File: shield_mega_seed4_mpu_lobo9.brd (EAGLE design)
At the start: 99.4 x 72.4 mm, 35 parts, among them U1 GY-521MPU6050

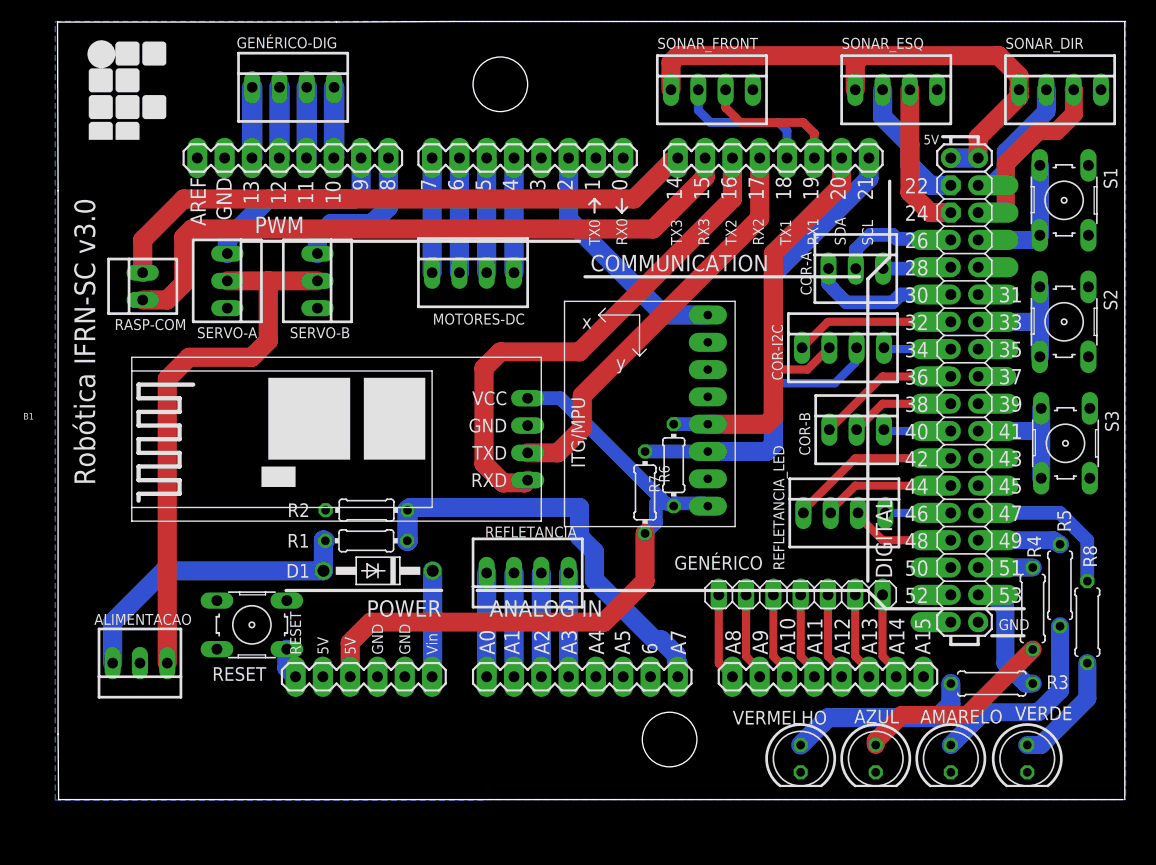
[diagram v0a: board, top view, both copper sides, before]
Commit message: Mudança de botões
mudança de posição nos botões
adição de conectores genéricos
adição de um quarto conector para sonares
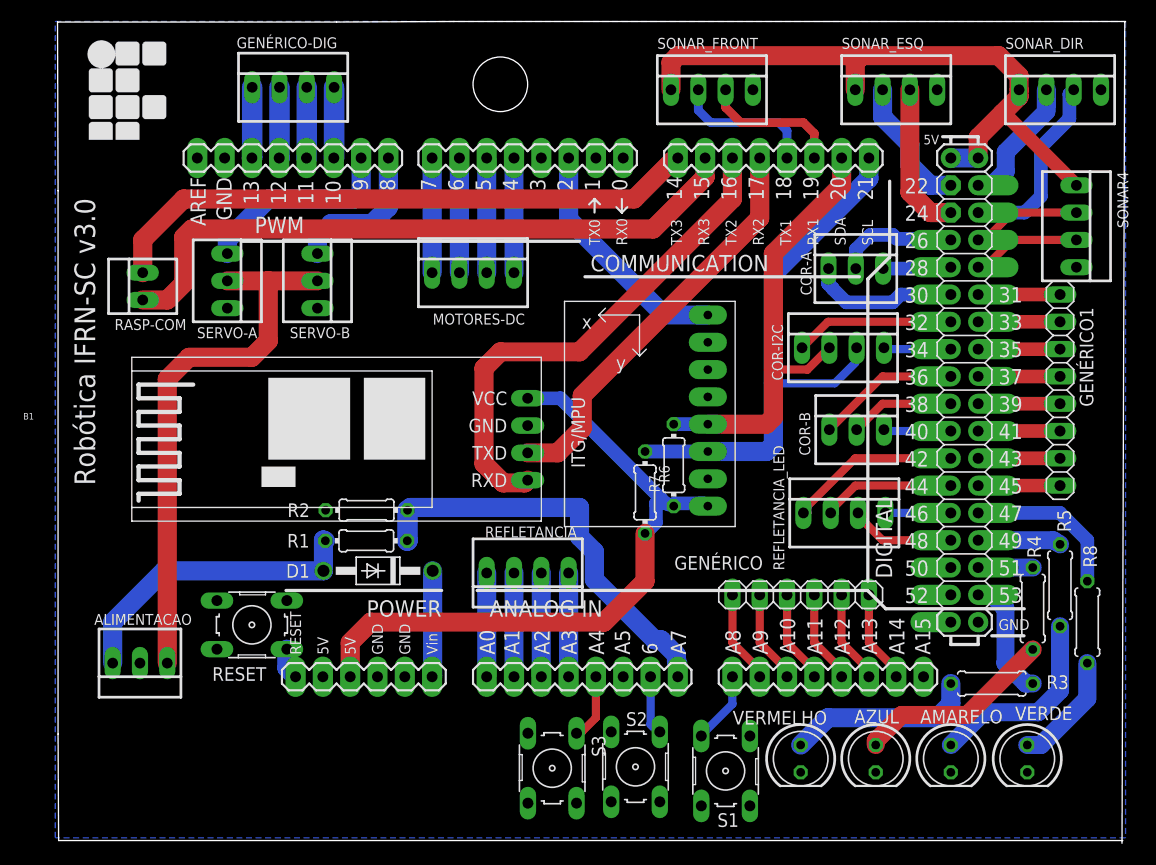
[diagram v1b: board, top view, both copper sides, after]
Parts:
- added GENÉRICO1: (no value), pinhead:1X08
- added SONAR4: (no value), con-molex:22-23-2041
- GENÉRICO: device pinhead:1X07 -> pinhead:1X06
- moved S1 61.7 mm to (61.6, 11.6), turned to 90 degrees
- moved S2 57.5 mm to (53.2, 11.9)
- moved S3 56.5 mm to (45.5, 11.8)
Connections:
- new net N$59: B1.A4, S3.1
- new net N$60: B1.31, GENÉRICO1.1
- new net N$61: B1.33, GENÉRICO1.2
- new net N$62: B1.35, GENÉRICO1.3
- new net N$63: B1.37, GENÉRICO1.4
- new net N$64: B1.39, GENÉRICO1.5
- new net N$65: B1.41, GENÉRICO1.6
- new net N$66: B1.43, GENÉRICO1.7
- new net N$67: B1.45, GENÉRICO1.8
- net 5V: now also SONAR4.1
- net GND: now also S1.3, S1.4, S2.3, S2.4, S3.3, S3.4, SONAR4.4; no longer S1.1, S1.2, S2.1, S2.2, S3.1, S3.2
- net N$27: now also B1.27, SONAR4.2; no longer B1.33, S2.3, S2.4
- net N$28: now also B1.A6, S2.1; no longer B1.27, S1.3, S1.4
- net N$30: now also B1.29, SONAR4.3; no longer B1.41, S3.3, S3.4
- net N$52: now also B1.A14, GENÉRICO.6; no longer B1.A8, GENÉRICO.1
- net N$53: now also B1.A13, GENÉRICO.5; no longer B1.A9, GENÉRICO.2
- net N$54: now also B1.A12, GENÉRICO.4; no longer B1.A10, GENÉRICO.3
- net N$55: now also GENÉRICO.3; no longer GENÉRICO.4
- net N$56: now also B1.A10, GENÉRICO.2; no longer B1.A12, GENÉRICO.5
- net N$57: now also B1.A9, GENÉRICO.1; no longer B1.A13, GENÉRICO.6
- net N$58: now also B1.A8, S1.2; no longer B1.A14, GENÉRICO.7
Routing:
- net 5V: track 51.0 -> 60.7 mm
- net N$67: track 0.00 -> 7.62 mm
- net N$66: track 0.00 -> 7.62 mm
- net N$65: track 0.00 -> 7.62 mm
- net N$64: track 0.00 -> 7.62 mm
- net N$63: track 0.00 -> 7.62 mm
- net N$62: track 0.00 -> 7.62 mm
- net N$61: track 0.00 -> 7.62 mm
- net N$60: track 0.00 -> 7.62 mm
- net N$28: track 12.4 -> 5.58 mm
- net N$59: track 0.00 -> 6.17 mm
- net N$30: track 12.4 -> 10.2 mm
- net N$27: track 12.3 -> 10.2 mm
- net N$58: track 8.15 -> 6.69 mm
- net N$56: track 8.15 -> 8.67 mm
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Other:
- board size 99.4 x 72.4 mm -> 99.4 x 76.5 mm

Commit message: Adição de conectores
Adição dos conectores de alimentação genéricos
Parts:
- added ALIMENTAÇÃO: (no value), pinhead:2X06
- moved GENÉRICO1 1.02 mm to (93.7, 47.0)
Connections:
- removed net N$32: B1.VIN, D1.C
- new net +3V3: ALIMENTAÇÃO.5, ALIMENTAÇÃO.6, B1.3.3V
- new net V+: ALIMENTAÇÃO.11, ALIMENTAÇÃO.12, B1.VIN, D1.C
- net +5V/1: now also ALIMENTAÇÃO.7, ALIMENTAÇÃO.8
- net GND: now also ALIMENTAÇÃO.10, ALIMENTAÇÃO.9
- net VDD: now also ALIMENTAÇÃO.3, ALIMENTAÇÃO.4
- net VIN: now also ALIMENTAÇÃO.1, ALIMENTAÇÃO.2
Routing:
- net VIN: track 28.5 -> 48.6 mm
- net V+: track 0.00 -> 18.8 mm
- net VDD: track 51.3 -> 69.1 mm
- net N$32: track 9.88 -> 0.00 mm
- net +5V/1: track 62.4 -> 70.2 mm
- net GND: track 0.38 -> 8.26 mm
- net +3V3: track 0.00 -> 7.87 mm
- net N$67: track 7.62 -> 8.64 mm
- net N$66: track 7.62 -> 8.64 mm
- net N$65: track 7.62 -> 8.64 mm
- net N$64: track 7.62 -> 8.64 mm
- net N$63: track 7.62 -> 8.64 mm
- net N$62: track 7.62 -> 8.64 mm
- net N$61: track 7.62 -> 8.64 mm
- net N$60: track 7.62 -> 8.64 mm
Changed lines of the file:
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@@
 <attribute name="VALUE" x="89.154" y="67.31" size="1.016" layer="27" ratio="10" rot="R270"/>
 </element>
-<element name="GENÉRICO1" library="pinhead" library_urn="urn:adsk.eagle:library:325" package="1X08" package3d_urn="urn:adsk.eagle:package:22409/2" value="" x="92.71" y="46.99" smashed="yes" rot="R270">
-<attribute name="NAME" x="94.5388" y="54.6862" size="1.27" layer="25" ratio="10" rot="R270"/>
-<attribute name="VALUE" x="89.535" y="54.61" size="1.27" layer="27" rot="R270"/>
+<element name="GENÉRICO1" library="pinhead" library_urn="urn:adsk.eagle:library:325" package="1X08" package3d_urn="urn:adsk.eagle:package:22409/2" value="" x="93.726" y="46.99" smashed="yes" rot="R270">
+<attribute name="NAME" x="95.5548" y="54.6862" size="1.27" layer="25" ratio="10" rot="R270"/>
+<attribute name="VALUE" x="90.551" y="54.61" size="1.27" layer="27" rot="R270"/>
+</element>
+<element name="ALIMENTAÇÃO" library="pinhead" library_urn="urn:adsk.eagle:library:325" package="2X06" package3d_urn="urn:adsk.eagle:package:22474/2" value="" x="25.4" y="13.716" smashed="yes">
+<attribute name="NAME" x="19.558" y="9.271" size="1.27" layer="25" ratio="10"/>
+<attribute name="VALUE" x="20.32" y="9.271" size="1.27" layer="27"/>
 </element>
 </elements>
@@
 <wire x1="50.8" y1="15.24" x2="50.9524" y2="15.1892" width="0.762" layer="16"/>
 <wire x1="50.8" y1="15.24" x2="50.9524125" y2="15.24" width="0.762" layer="16"/>
+<contactref element="ALIMENTAÇÃO" pad="10"/>
+<contactref element="ALIMENTAÇÃO" pad="9"/>
+<wire x1="29.21" y1="20.32" x2="29.21" y2="14.986" width="1.78" layer="16"/>
+<wire x1="29.21" y1="14.986" x2="29.21" y2="12.446" width="1.78" layer="16"/>
 </signal>
 <signal name="VIN">
@@
 <wire x1="24.1808" y1="30.1752" x2="24.1808" y2="33.0454" width="1.778" layer="16"/>
 <wire x1="24.1808" y1="33.0454" x2="24.3586" y2="32.9692" width="1.778" layer="16"/>
+<contactref element="ALIMENTAÇÃO" pad="2"/>
+<contactref element="ALIMENTAÇÃO" pad="1"/>
+<wire x1="19.05" y1="14.986" x2="19.05" y2="12.446" width="1.27" layer="1"/>
+<wire x1="19.05" y1="14.986" x2="19.05" y2="15.494" width="1.27" layer="1"/>
+<wire x1="5.215" y1="20.80423125" x2="5.215" y2="20.947" width="1.27" layer="1"/>
+<wire x1="5.215" y1="20.947" x2="4.572" y2="21.59" width="1.27" layer="1"/>
+<wire x1="17.78" y1="16.764" x2="9.25523125" y2="16.764" width="1.27" layer="1"/>
+<wire x1="9.25523125" y1="16.764" x2="5.215" y2="20.80423125" width="1.27" layer="1"/>
+<wire x1="19.05" y1="15.494" x2="17.78" y2="16.764" width="1.27" layer="1"/>
 </signal>
 <signal name="VDD">
@@
 <wire x1="17.526" y1="50.038" x2="19.05" y2="51.562" width="1.778" layer="1"/>
 <wire x1="19.05" y1="51.562" x2="19.05" y2="57.15" width="1.778" layer="1"/>
+<contactref element="ALIMENTAÇÃO" pad="4"/>
+<contactref element="ALIMENTAÇÃO" pad="3"/>
+<wire x1="9.652" y1="21.59" x2="12.7" y2="18.542" width="1.27" layer="1"/>
+<wire x1="19.05" y1="18.542" x2="21.59" y2="16.002" width="1.27" layer="1"/>
+<wire x1="21.59" y1="16.002" x2="21.59" y2="14.986" width="1.27" layer="1"/>
+<wire x1="12.7" y1="18.542" x2="19.05" y2="18.542" width="1.27" layer="1"/>
+<wire x1="21.59" y1="14.986" x2="21.59" y2="12.446" width="1.27" layer="1"/>
 </signal>
 <signal name="+IN">
@@
 <wire x1="54.102" y1="33.655" x2="55.118" y2="34.671" width="1.27" layer="16"/>
 <wire x1="55.118" y1="36.449" x2="55.5625" y2="36.8935" width="1.27" layer="16"/>
+<contactref element="ALIMENTAÇÃO" pad="8"/>
+<contactref element="ALIMENTAÇÃO" pad="7"/>
+<wire x1="26.67" y1="20.32" x2="26.67" y2="14.986" width="1.78" layer="16"/>
+<wire x1="26.67" y1="14.986" x2="26.67" y2="12.446" width="1.78" layer="16"/>
 </signal>
 <signal name="SCL">
@@
 <wire x1="82.423" y1="58.293" x2="82.55" y2="58.42" width="1.27" layer="16"/>
 </signal>
-<signal name="N$32">
-<contactref element="D1" pad="C"/>
-<contactref element="B1" pad="VIN"/>
-<wire x1="34.3408" y1="30.1752" x2="34.3408" y2="20.3708" width="1.778" layer="16"/>
-<wire x1="34.3408" y1="20.3708" x2="34.29" y2="20.32" width="1.778" layer="16"/>
-</signal>
 <signal name="N$38">
 <contactref element="B1" pad="47"/>
@@
 <contactref element="B1" pad="31"/>
 <contactref element="GENÉRICO1" pad="1"/>
-<wire x1="85.09" y1="55.88" x2="92.71" y2="55.88" width="1.27" layer="1"/>
+<wire x1="85.09" y1="55.88" x2="93.726" y2="55.88" width="1.27" layer="1"/>
 </signal>
 <signal name="N$61">
 <contactref element="B1" pad="33"/>
 <contactref element="GENÉRICO1" pad="2"/>
-<wire x1="85.09" y1="53.34" x2="92.71" y2="53.34" width="1.27" layer="1"/>
+<wire x1="85.09" y1="53.34" x2="93.726" y2="53.34" width="1.27" layer="1"/>
 </signal>
 <signal name="N$63">
 <contactref element="B1" pad="37"/>
 <contactref element="GENÉRICO1" pad="4"/>
-<wire x1="85.09" y1="48.26" x2="92.71" y2="48.26" width="1.27" layer="1"/>
+<wire x1="85.09" y1="48.26" x2="93.726" y2="48.26" width="1.27" layer="1"/>
 </signal>
 <signal name="N$64">
 <contactref element="B1" pad="39"/>
 <contactref element="GENÉRICO1" pad="5"/>
-<wire x1="85.09" y1="45.72" x2="92.71" y2="45.72" width="1.27" layer="1"/>
+<wire x1="85.09" y1="45.72" x2="93.726" y2="45.72" width="1.27" layer="1"/>
 </signal>
 <signal name="N$65">
 <contactref element="B1" pad="41"/>
 <contactref element="GENÉRICO1" pad="6"/>
-<wire x1="85.09" y1="43.18" x2="92.71" y2="43.18" width="1.27" layer="1"/>
+<wire x1="85.09" y1="43.18" x2="93.726" y2="43.18" width="1.27" layer="1"/>
 </signal>
 <signal name="N$62">
 <contactref element="B1" pad="35"/>
 <contactref element="GENÉRICO1" pad="3"/>
-<wire x1="85.09" y1="50.8" x2="92.71" y2="50.8" width="1.27" layer="1"/>
+<wire x1="85.09" y1="50.8" x2="93.726" y2="50.8" width="1.27" layer="1"/>
 </signal>
 <signal name="N$66">
 <contactref element="B1" pad="43"/>
 <contactref element="GENÉRICO1" pad="7"/>
-<wire x1="85.09" y1="40.64" x2="92.71" y2="40.64" width="1.27" layer="1"/>
+<wire x1="85.09" y1="40.64" x2="93.726" y2="40.64" width="1.27" layer="1"/>
 </signal>
 <signal name="N$67">
 <contactref element="B1" pad="45"/>
 <contactref element="GENÉRICO1" pad="8"/>
-<wire x1="85.09" y1="38.1" x2="92.71" y2="38.1" width="1.27" layer="1"/>
+<wire x1="85.09" y1="38.1" x2="93.726" y2="38.1" width="1.27" layer="1"/>
 </signal>
 <signal name="N$28">
@@
 <wire x1="55.245" y1="15.24" x2="55.4736" y2="15.1892" width="0.762" layer="16"/>
 </signal>
+<signal name="+3V3">
+<contactref element="B1" pad="3.3V"/>
+<contactref element="ALIMENTAÇÃO" pad="6"/>
+<contactref element="ALIMENTAÇÃO" pad="5"/>
+<wire x1="24.13" y1="20.32" x2="24.13" y2="14.986" width="1.78" layer="16"/>
+<wire x1="24.13" y1="14.986" x2="24.13" y2="12.446" width="1.78" layer="16"/>
+</signal>
+<signal name="V+">
+<contactref element="ALIMENTAÇÃO" pad="11"/>
+<contactref element="ALIMENTAÇÃO" pad="12"/>
+<contactref element="D1" pad="C"/>
+<contactref element="B1" pad="VIN"/>
+<wire x1="34.3408" y1="30.1752" x2="34.3408" y2="20.3708" width="1.778" layer="16"/>
+<wire x1="34.3408" y1="20.3708" x2="34.29" y2="20.32" width="1.778" layer="16"/>
+<wire x1="34.29" y1="20.32" x2="34.29" y2="18.034" width="1.75" layer="16"/>
+<wire x1="34.29" y1="18.034" x2="31.75" y2="15.494" width="1.75" layer="16"/>
+<wire x1="31.75" y1="15.494" x2="31.75" y2="14.986" width="1.75" layer="16"/>
+<wire x1="31.75" y1="14.986" x2="31.75" y2="12.446" width="1.75" layer="16"/>
+</signal>
 </signals>

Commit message: Adição de logo
modificação de logo do IF
adição na parte superior da placa de logos da robótica
adição de imagens dos logos
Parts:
- added GENÉRICO2: (no value), pinhead:1X03
- renumbered GENÉRICO-DIG to GENÉRICO3
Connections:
- new net N$32: B1.0, GENÉRICO2.1
- new net N$68: B1.1, GENÉRICO2.2
- new net N$69: B1.3, GENÉRICO2.3
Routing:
- net N$69: track 0.00 -> 7.40 mm
- net N$68: track 0.00 -> 6.35 mm
- net N$32: track 0.00 -> 6.35 mm
- net N$20: track 39.0 -> 37.6 mm

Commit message: Adição de novo layer
Adição de novo layer para os logos
Organização de nomes dos componetes
Pequena modificação do botões para alinha-los
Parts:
- removed GENÉRICO2: (no value), pinhead:1X03
- added GENERICO2: (no value), pinhead:1X03
- moved S3 0.76 mm to (44.7, 11.8)
- moved S1 0.38 mm to (61.6, 11.9)
- moved S2 0.25 mm to (53.0, 11.9)
- renumbered ALIMENTAÇÃO to CON_ALIMENTACAO, GENÉRICO to GENERICO, GENÉRICO3 to GENERICO3
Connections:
- net N$32: now also GENERICO2.1; no longer GENÉRICO2.1
- net N$68: now also GENERICO2.2; no longer GENÉRICO2.2
- net N$69: now also GENERICO2.3; no longer GENÉRICO2.3
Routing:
- net N$69: track 7.40 -> 6.35 mm
- net N$68: track 6.35 -> 7.40 mm
- net N$32: track 6.35 -> 7.40 mm
